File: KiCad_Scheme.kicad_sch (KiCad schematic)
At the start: 1 part

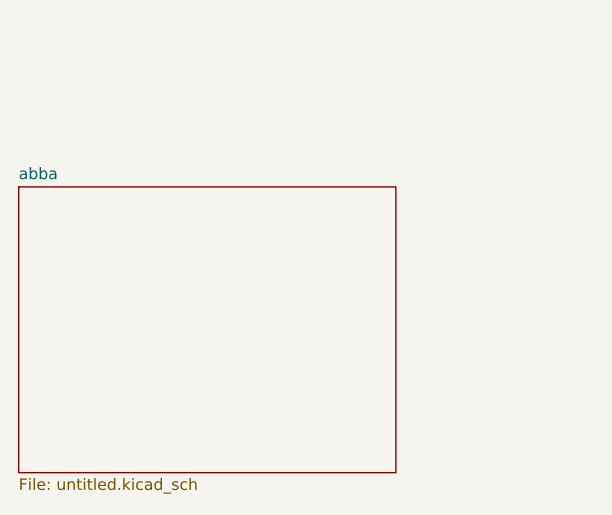
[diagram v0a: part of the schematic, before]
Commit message: version: Upgrade to KiCad 9
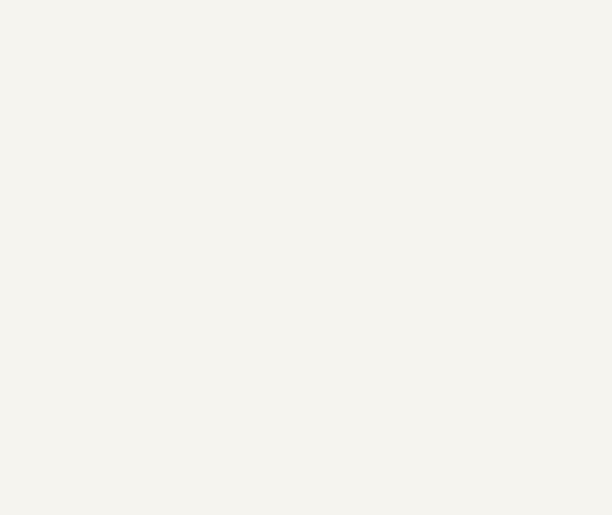
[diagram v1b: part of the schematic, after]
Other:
- removed sheet abba
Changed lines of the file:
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@@
 (kicad_sch
-	(version 20231120)
+	(version 20250114)
 	(generator "eeschema")
-	(generator_version "8.0")
+	(generator_version "9.0")
 	(paper "A4")
 	(symbol
@@
 		)
 	)
-	(sheet
-		(at 86.36 64.77)
-		(size 41.91 31.75)
-		(fields_autoplaced yes)
-		(stroke
-			(width 0.1524)
-			(type solid)
-		)
-		(fill
-			(color 0 0 0 0.0000)
-		)
-		(property "Sheetname" "abba"
-			(at 86.36 64.0584 0)
-			(effects
-				(font
-					(size 1.27 1.27)
-				)
-				(justify left bottom)
-			)
-		)
-		(property "Sheetfile" "untitled.kicad_sch"
-			(at 86.36 97.1046 0)
-			(effects
-				(font
-					(size 1.27 1.27)
-				)
-				(justify left top)
-			)
-		)
-		(instances
-			(project ""
-				(path "/e99fb634-873d-43be-86a6-ee1889cd3062"
-					(page "2")
-				)
-			)
-		)
-	)
 	(sheet_instances
 		(path "/"
@@
 		)
 	)
+	(embedded_fonts no)
 )
